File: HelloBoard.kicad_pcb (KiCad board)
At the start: 2 copper layers, 36 parts, among them J1 USB_B_Micro, J2 Conn_01x04_Pin, J3 Conn_01x04_Pin, J4 Conn_02x08_Top_Bottom, SW1 SW_Push, SW2 SW_Push, U1 STM32F103C8T6, U2 AMS1117-3.3, U3 TMP235A2DCKR, U4 ADXL343, U5 DA56-11CGKWA, Y1 16MHz

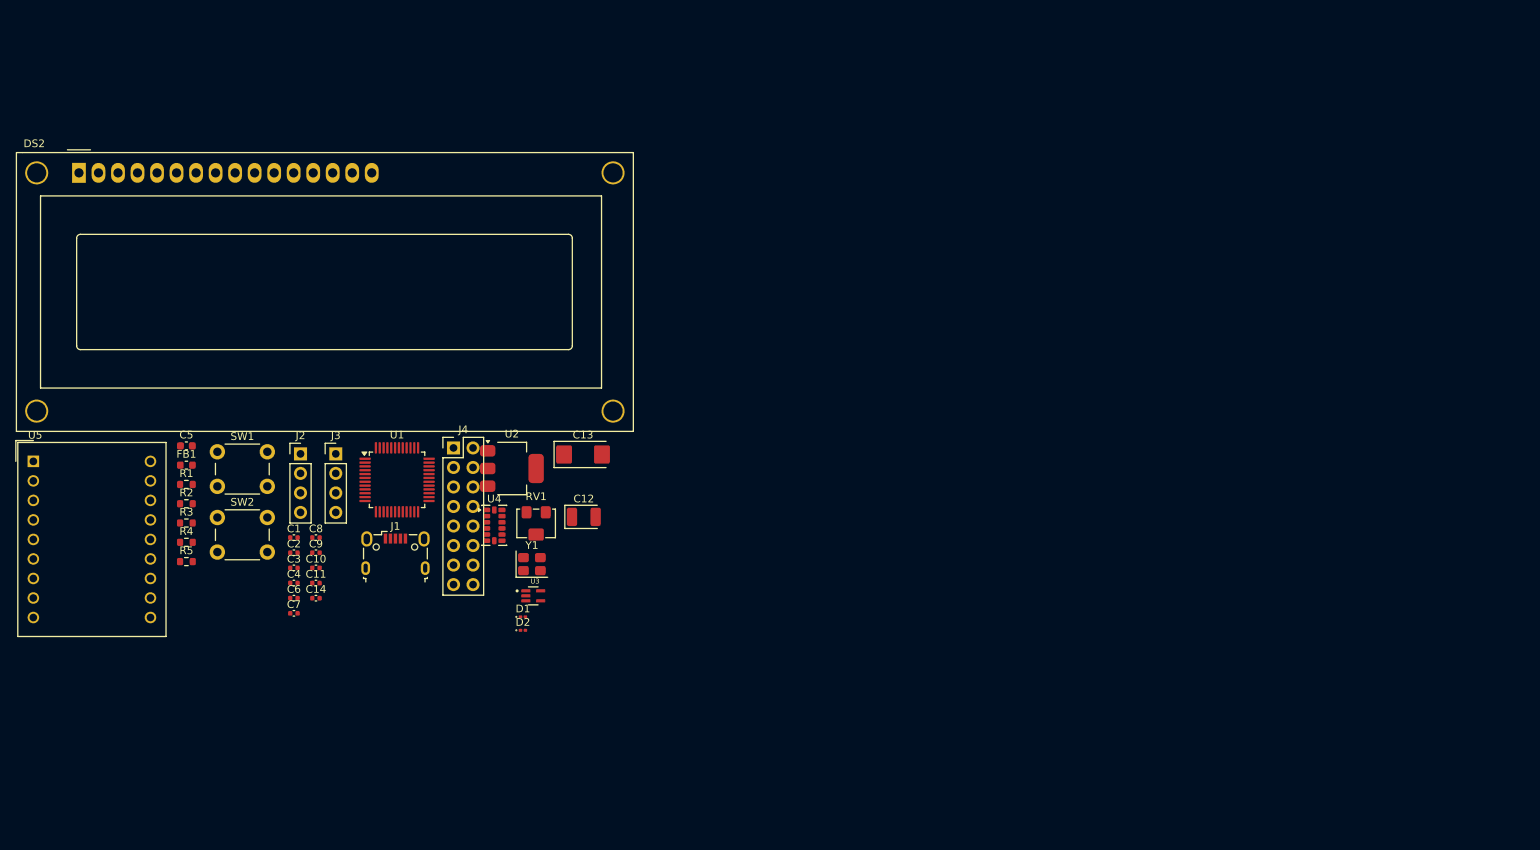
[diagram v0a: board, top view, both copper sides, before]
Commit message: added SilkScreen images and external pulldown for user button
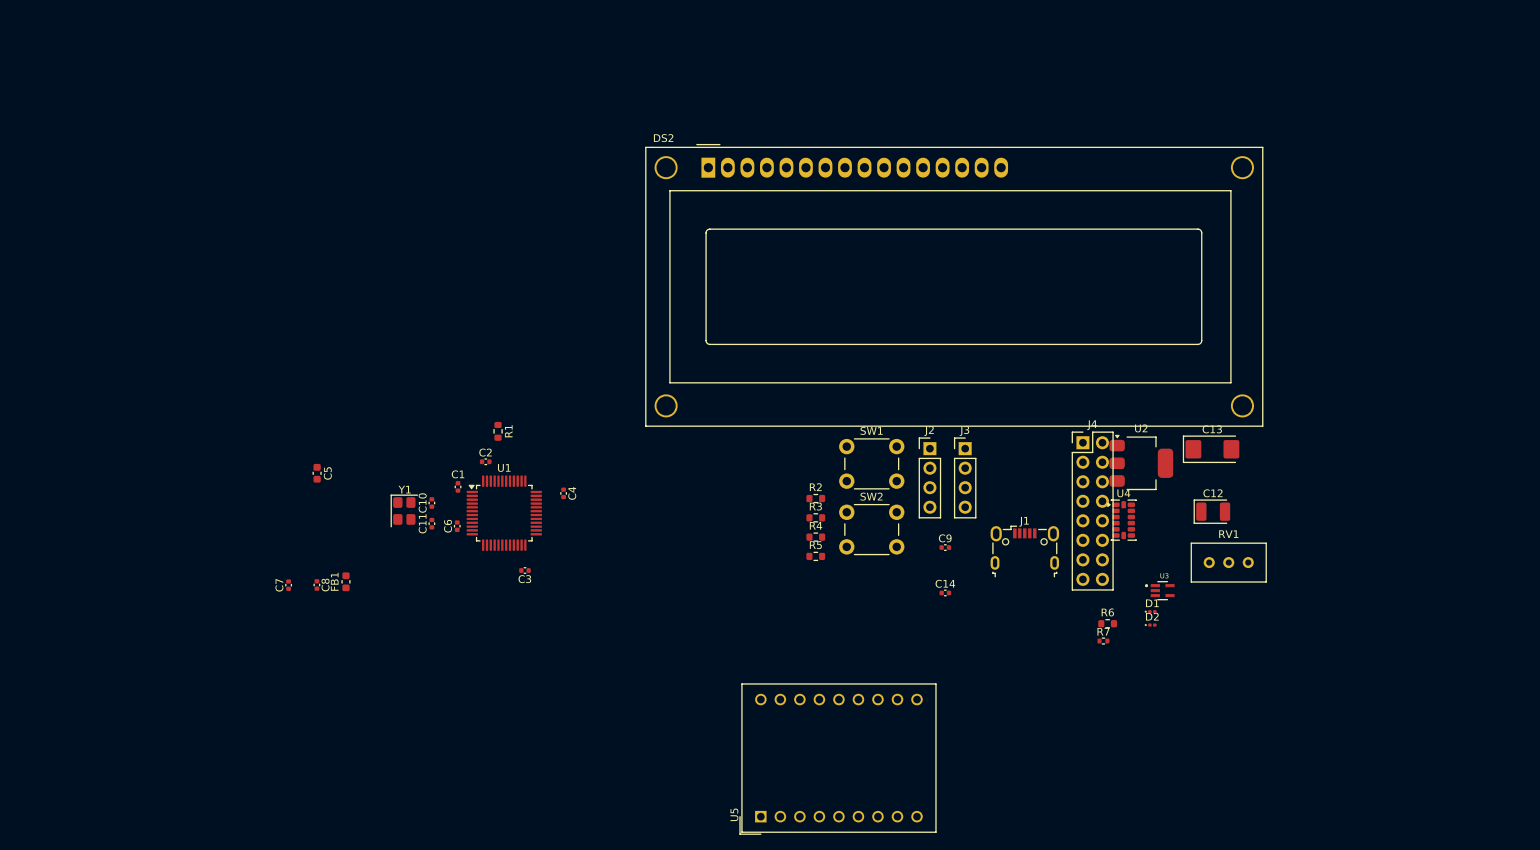
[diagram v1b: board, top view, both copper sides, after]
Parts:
- added G***: LOGO, SilkScreen:potatoblood, B.Cu at (179.4, 55.2)
- added G***: LOGO, SilkScreen:toothless, B.Cu at (130.8, 52.1)
- added G***: LOGO, SilkScreen:kirby, B.Cu at (138.7, 57.1)
- added G***: LOGO, SilkScreen:puck, B.Cu at (164.0, 47.9)
- added G***: LOGO, SilkScreen:bob, B.Cu at (151.0, 66.3)
- added G***: LOGO, SilkScreen:omarqm, B.Cu at (143.1, 47.4)
- added G***: LOGO, SilkScreen:theo, B.Cu at (162.1, 59.0)
- added G***: LOGO, SilkScreen:mnrn, B.Cu at (171.2, 55.2)
- added G***: LOGO, SilkScreen:turtle, B.Cu at (150.8, 56.2)
- added G***: LOGO, SilkScreen:kuriboh, B.Cu at (155.7, 47.8)
- added G***: LOGO, SilkScreen:asha, B.Cu at (123.1, 56.8)
- added R6: 10k, Resistor_SMD:R_0603_1608Metric, F.Cu at (170.7, 100.1)
- added R7: 330, Resistor_SMD:R_0402_1005Metric, F.Cu at (170.2, 102.4)
- RV1: footprint Potentiometer_SMD:Potentiometer_Bourns_3214W_Vertical -> Potentiometer_THT:Potentiometer_Bourns_3296W_Vertical
- moved U5 105.4 mm to (125.6, 125.2), turned to 90 degrees
- moved RV1 92.8 mm to (189.0, 92.2)
- moved C12 81.9 mm to (184.5, 85.6)
- moved J2 81.9 mm to (147.6, 77.4)
- moved J3 81.9 mm to (152.2, 77.4)
- moved R2 81.9 mm to (132.8, 83.9)
- moved R3 81.9 mm to (132.8, 86.4)
- moved R4 81.9 mm to (132.8, 88.9)
- moved R5 81.9 mm to (132.8, 91.4)
- moved SW1 81.9 mm to (136.8, 77.1)
- moved SW2 81.9 mm to (136.8, 85.6)
- moved U4 81.9 mm to (172.8, 86.7)
- moved C13 81.9 mm to (184.4, 77.4)
- moved C14 81.9 mm to (149.6, 96.1)
- moved C9 81.9 mm to (149.6, 90.2)
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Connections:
- SW2 pad 2: /USER_BUTTON -> Net-(R6-Pad1)

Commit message: swapped 7Seg footprint
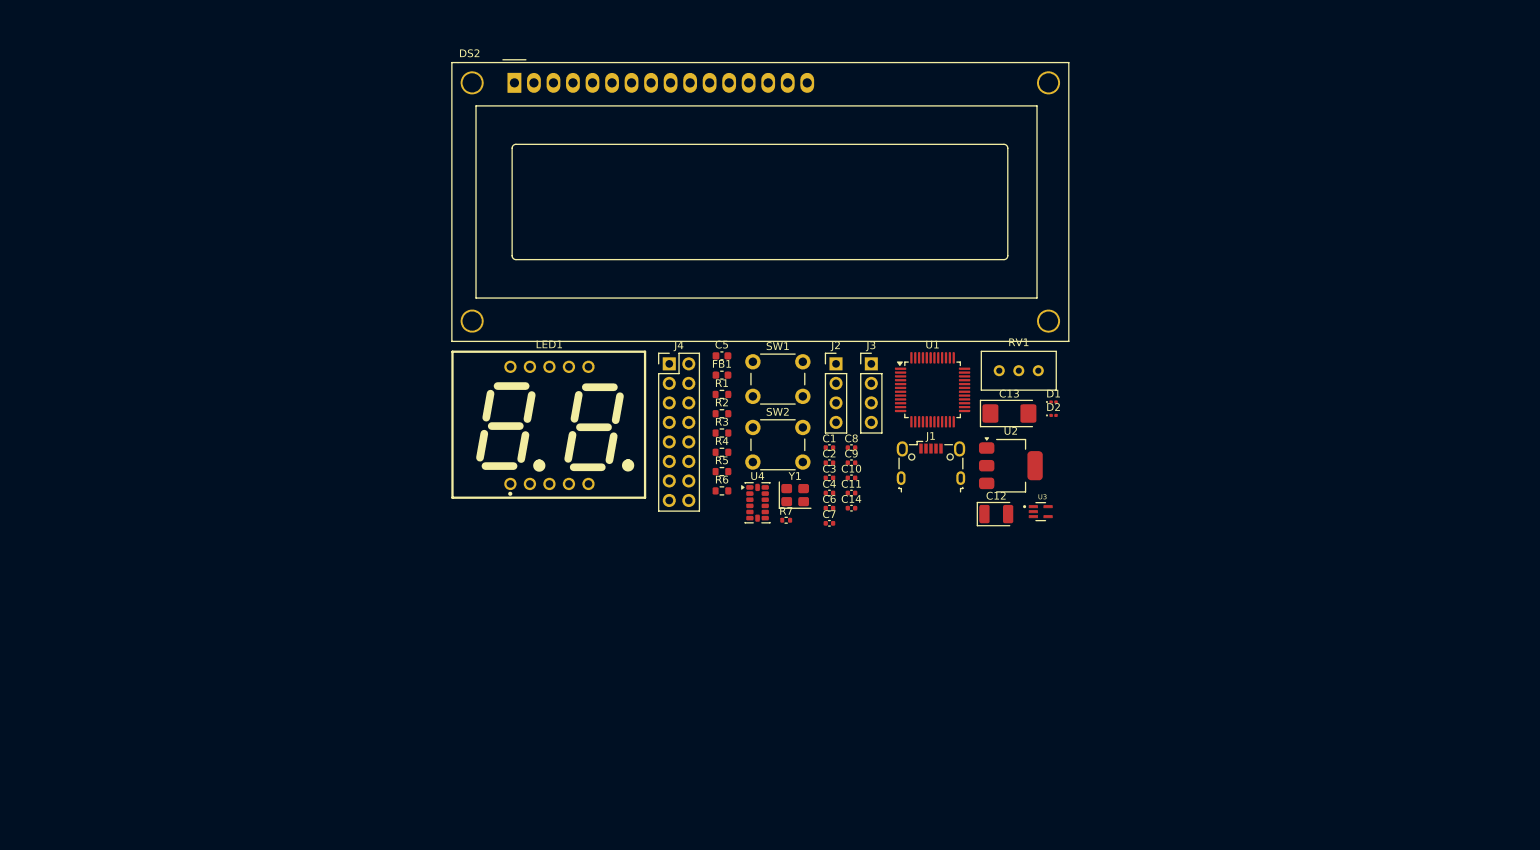
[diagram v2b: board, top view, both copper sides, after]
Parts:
- removed G***: LOGO, SilkScreen:potatoblood
- removed G***: LOGO, SilkScreen:toothless
- removed G***: LOGO, SilkScreen:kirby
- removed G***: LOGO, SilkScreen:puck
- removed G***: LOGO, SilkScreen:bob
- removed G***: LOGO, SilkScreen:omarqm
- removed G***: LOGO, SilkScreen:theo
- removed G***: LOGO, SilkScreen:mnrn
- removed G***: LOGO, SilkScreen:turtle
- removed G***: LOGO, SilkScreen:kuriboh
- removed G***: LOGO, SilkScreen:asha
- removed U5: DA56-11CGKWA, Display_7Segment:DA56-11CGKWA
- added LED1: ~, 7Segment2Digit:7Segment2Digit, F.Cu at (98.1, 74.3)
- moved C8 71.8 mm to (137.4, 77.2), turned to 0 degrees
- moved C7 70.8 mm to (134.5, 87.1), turned to 0 degrees
- moved U1 58.0 mm to (148.0, 69.7)
- moved FB1 55.8 mm to (120.5, 67.8), turned to 0 degrees
- moved C5 54.8 mm to (120.5, 65.3), turned to 0 degrees
- moved J4 54.8 mm to (113.7, 66.3)
- moved C11 54.7 mm to (137.4, 83.1), turned to 0 degrees
- moved C10 54.7 mm to (137.4, 81.2), turned to 0 degrees
- moved R6 53.1 mm to (120.5, 82.9)
- moved Y1 50.9 mm to (130.1, 83.4), turned to 0 degrees
- moved C1 48.6 mm to (134.5, 77.2), turned to 0 degrees
- moved C6 48.5 mm to (134.5, 85.1), turned to 0 degrees
- moved U4 47.7 mm to (125.2, 84.4)
- moved C2 44.7 mm to (134.5, 79.2)
- moved R7 44.2 mm to (128.9, 86.7)
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
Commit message: started rough layout
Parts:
- added H1: MountingHole, MountingHole:MountingHole_2.2mm_M2, F.Cu at (171.9, 24.7)
- added H2: MountingHole, MountingHole:MountingHole_2.2mm_M2, F.Cu at (81.9, 24.7)
- added H3: MountingHole, MountingHole:MountingHole_2.2mm_M2, F.Cu at (81.9, 89.7)
- added H4: MountingHole, MountingHole:MountingHole_2.2mm_M2, F.Cu at (171.9, 89.7)
- GPIO HEADER: renamed from J4
- I2C HEADER: renamed from J3
- SWD HEADER: renamed from J2
- USB CONNECTOR: renamed from J1
- moved USER_LED 83.5 mm to (81.2, 85.3)
- moved POWER_LED 83.2 mm to (81.2, 82.2)
- moved U3 56.7 mm to (110.9, 61.1)
- moved GPIO HEADER 34.4 mm to (86.6, 87.5), turned to 90 degrees
- moved USB CONNECTOR 27.5 mm to (170.9, 64.4), turned to 90 degrees
- moved LCD_CONTRAST 26.8 mm to (171.1, 42.1), turned to 90 degrees
- moved RESET 24.3 mm to (109.6, 85.2)
- moved I2C HEADER 21.6 mm to (144.3, 87.5), turned to 90 degrees
- moved SWD HEADER 21.6 mm to (131.3, 87.5), turned to 90 degrees
- moved U4 18.5 mm to (126.7, 66.0)
- moved Y1 16.6 mm to (132.5, 67.0)
- moved R7 12.0 mm to (130.3, 74.7)
- moved USER_BUTTON 11.8 mm to (119.5, 85.3)
- moved U2 11.7 mm to (169.5, 82.4)
- moved C13 11.1 mm to (168.5, 76.2)
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- renumbered RV1 to LCD_CONTRAST, D1 to POWER_LED, SW1 to RESET, SW2 to USER_BUTTON, D2 to USER_LED
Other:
- board outline added: 96 x 71 mm
- board text added: "3.3V"
- board text added: "5V"
- board text added: "7 SEGMENT DISPLAY"
- board text added: "GND"
- board text added: "PA_10"
- board text added: "PA_11"
- board text added: "PA_12"
- board text added: "PA_7"
- board text added: "PA_8"
- board text added: "PA_9"
- board text added: "PB_1"
- board text added: "PB_2"
- board text added: "PB_3"
- board text added: "PB_4"
- board text added: "PB_5"
- board text added: "PC_14"
- board text added: "PC_15"
- board text added: "SCL"
- board text added: "SDA"
- board text added: "SWCLK"
- board text added: "SWDIO"

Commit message: basic placement done
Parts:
- added J5: Conn_01x02, Connector_PinHeader_2.54mm:PinHeader_1x02_P2.54mm_Vertical, F.Cu at (172.0, 83.6)
- J1: renamed from USB CONNECTOR
- J2: renamed from SWD HEADER
- J3: renamed from I2C HEADER
- J4: renamed from GPIO HEADER
- moved U4 45.8 mm to (166.4, 89.0)
- moved R3 36.8 mm to (80.7, 81.8)
- moved R5 36.4 mm to (80.6, 85.3)
- moved R6 35.5 mm to (151.1, 80.6)
- moved U3 26.3 mm to (130.7, 78.4)
- moved SW2 25.8 mm to (145.3, 85.1)
- moved C12 24.8 mm to (160.7, 63.9), turned to 90 degrees
- moved SW1 24.1 mm to (133.7, 85.1)
- moved U2 21.2 mm to (154.0, 67.9), turned to 180 degrees
- moved C11 20.1 mm to (123.5, 67.0), turned to 90 degrees
- moved R2 19.2 mm to (128.2, 82.9)
- moved U1 18.2 mm to (131.9, 68.2)
- moved C4 17.9 mm to (125.9, 64.9), turned to 90 degrees
- moved C10 17.9 mm to (123.5, 69.3), turned to -90 degrees
- moved R7 17.7 mm to (146.8, 80.9)
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- renumbered POWER_LED to D1, USER_LED to D2, LCD_CONTRAST to RV1, RESET to SW1, USER_BUTTON to SW2
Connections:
- net Net-(D2-K) renamed /USER_LED_K
- net Net-(R6-Pad1) renamed /NODE_USER_BUTTON
- U4 pad 8: unconnected-(U4-INT1-Pad8) -> Net-(J5-Pin_1)
- U4 pad 9: unconnected-(U4-INT2-Pad9) -> Net-(J5-Pin_2)

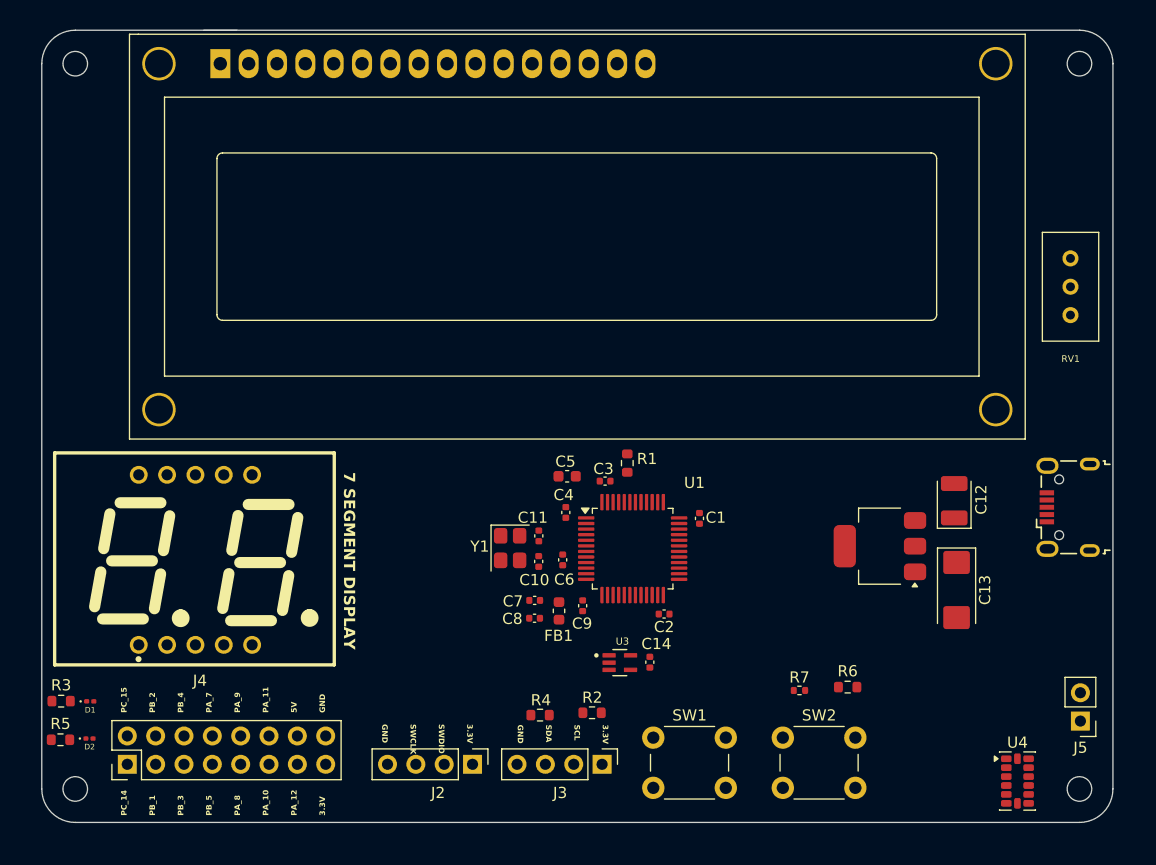
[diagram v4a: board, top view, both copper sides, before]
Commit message: added ground plane
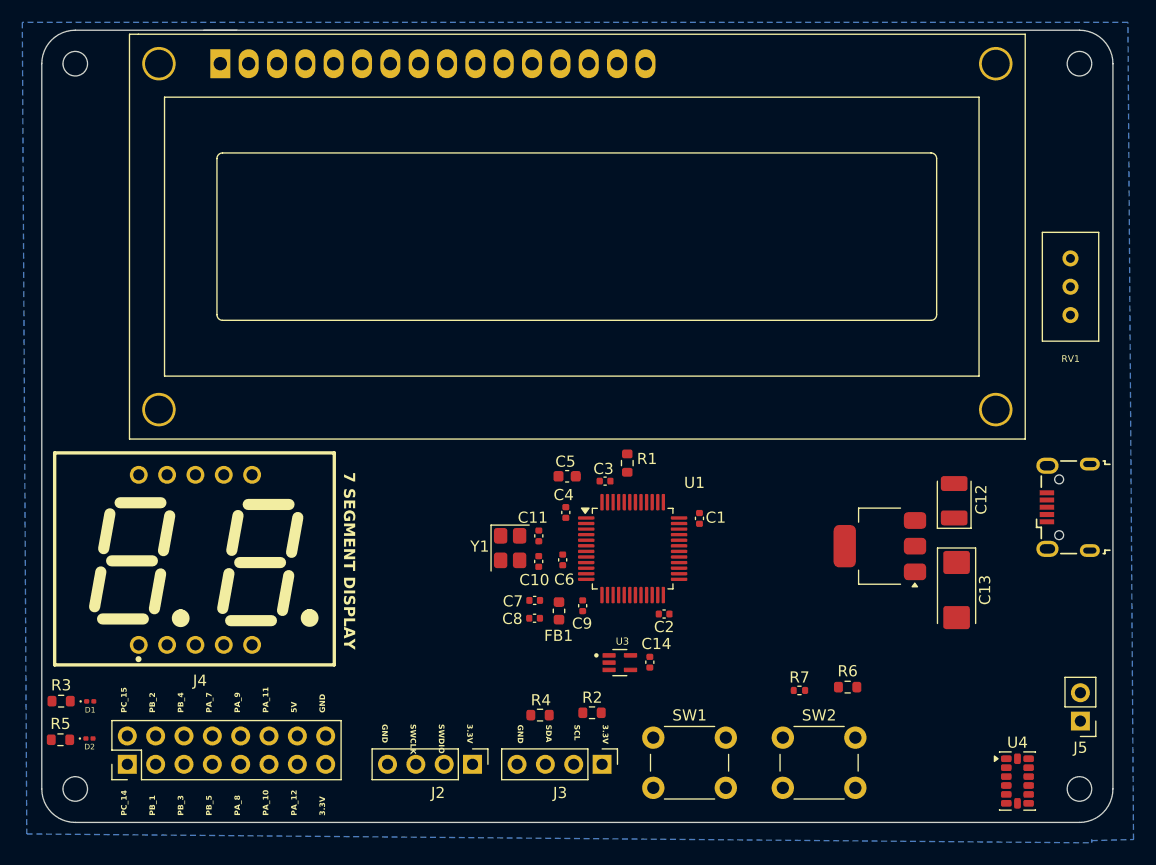
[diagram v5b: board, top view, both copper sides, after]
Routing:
- added copper zone on B.Cu, net GND
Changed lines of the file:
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@@
+		)
+	)
+	(zone
+		(net 1)
+		(net_name "GND")
+		(layer "B.Cu")
+		(hatch edge 0.5)
+		(connect_pads
+			(clearance 0.5)
+		)
+		(min_thickness 0.25)
+		(filled_areas_thickness no)
+		(fill yes
+			(thermal_gap 0.5)
+			(thermal_bridge_width 0.5)
+		)
+		(polygon
+			(pts
+				(xy 173.015 94.32) (xy 176.76 94.22) (xy 176.26 20.98) (xy 77.17 20.98) (xy 77.57 93.72) (xy 173.015 94.52)
+				(xy 173.015 94.23)
+			)
 		)
 	)

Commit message: added "power puddles" shoutout phil's lab
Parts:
- moved J1 88.6 mm to (82.4, 62.6), turned to -90 degrees
- moved C12 68.5 mm to (92.3, 61.1), turned to 0 degrees
- moved C13 61.4 mm to (99.7, 66.9), turned to 90 degrees
- moved LED1 61.0 mm to (153.7, 70.1)
- moved U2 60.9 mm to (93.2, 67.5), turned to -90 degrees
- moved SW1 8.71 mm to (141.2, 89.6), turned to 180 degrees
- moved SW2 7.39 mm to (151.2, 89.6), turned to 180 degrees
- moved R6 2.51 mm to (149.5, 82.5)
- moved R7 2.04 mm to (145.6, 82.5)
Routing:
- net GND: track 0.00 -> 40.8 mm, vias 0 -> 15
- added copper zone on F.Cu, net +3.3V
- added copper zone on F.Cu, net GND
- added copper zone on F.Cu, net VBUS

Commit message: حلتيته
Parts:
- D1, D2: footprint LED_SMD:LED_0201_0603Metric -> LED_SMD:LED_0603_1608Metric
- moved H3 145.4 mm to (218.9, 41.0)
- moved J4 111.0 mm to (189.4, 45.5)
- moved H2 94.7 mm to (118.6, 112.0)
- moved J2 77.2 mm to (180.6, 43.0)
- moved DS2 69.9 mm to (136.7, 80.7)
- moved RV1 66.1 mm to (123.0, 87.5)
- moved J3 58.8 mm to (167.6, 43.0)
- moved H1 55.8 mm to (118.6, 41.0)
- moved D2 54.5 mm to (127.3, 53.2)
- moved R5 53.6 mm to (123.6, 53.2)
- moved SW2 53.3 mm to (125.7, 42.7), turned to 0 degrees
- moved R2 53.0 mm to (167.7, 47.5), turned to 180 degrees
- moved H4 52.0 mm to (218.9, 112.0)
- moved R4 51.9 mm to (160.3, 46.4), turned to 0 degrees
- moved D1 50.8 mm to (127.3, 56.5)
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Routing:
- net VBUS: track 0.00 -> 87.9 mm
- net +3.3V: track 0.00 -> 35.8 mm
- net /NRST: track 0.00 -> 33.7 mm
- net /LCD_RS: track 0.00 -> 28.7 mm
- net GND: track 40.8 -> 67.0 mm, vias 15 -> 24
- net /SWDIO: track 0.00 -> 24.7 mm
- net /SWCLK: track 0.00 -> 23.5 mm
- net /LCD_VO: track 0.00 -> 22.7 mm
- net /I2C_SDA: track 0.00 -> 22.7 mm
- net /LCD_E: track 0.00 -> 19.7 mm
- net /LCD_D7: track 0.00 -> 19.2 mm
- net /I2C_SCL: track 0.00 -> 19.0 mm
- net /LCD_D6: track 0.00 -> 17.8 mm
- net /LCD_D5: track 0.00 -> 17.0 mm
- net /LCD_D4: track 0.00 -> 16.1 mm
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- removed copper zone on F.Cu, net +3.3V
- removed copper zone on F.Cu, net GND
- removed copper zone on F.Cu, net VBUS
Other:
- board size 96 x 71 mm -> 106.3 x 77 mm
- board text removed: "3.3V"
- board text removed: "5V"
- board text removed: "7 SEGMENT DISPLAY"
- board text removed: "GND"
- board text removed: "PA_10"
- board text removed: "PA_11"
- board text removed: "PA_12"
- board text removed: "PA_7"
- board text removed: "PA_8"
- board text removed: "PA_9"
- board text removed: "PB_1"
- board text removed: "PB_2"
- board text removed: "PB_3"
- board text removed: "PB_4"
- board text removed: "PB_5"
- board text removed: "PC_14"
- board text removed: "PC_15"
- board text removed: "SCL"
- board text removed: "SDA"
- board text removed: "SWCLK"
- board text removed: "SWDIO"
